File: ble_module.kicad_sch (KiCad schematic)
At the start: 2 parts, among them U1 STM32WB55RCVx, Y1 Crystal

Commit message: 3/8/2025
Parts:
- added C1, C2, C3, C4: 6 pF, Capacitor_SMD:C_0603_1608Metric, symbol Device:C
- added J1, J11: Conn_01x06_Pin, Connector_PinHeader_2.54mm:PinHeader_1x06_P2.54mm_Vertical, symbol Connector:Conn_01x06_Pin
- added J10: Conn_01x04_Pin, Connector_PinHeader_2.54mm:PinHeader_1x04_P2.54mm_Vertical, symbol Connector:Conn_01x04_Pin
- added J2: Conn_02x05_Odd_Even, Connector_PinHeader_1.27mm:PinHeader_2x05_P1.27mm_Vertical, symbol Connector_Generic:Conn_02x05_Odd_Even
- added J8: Conn_01x02_Pin, Connector_PinHeader_2.54mm:PinHeader_1x02_P2.54mm_Vertical, symbol Connector:Conn_01x02_Pin
- added J9: Conn_01x06_Pin, Connector_PinHeader_2.54mm:PinHeader_2x03_P2.54mm_Vertical, symbol Connector:Conn_01x06_Pin
- added R1, R2: 10k, Resistor_SMD:R_0603_1608Metric, symbol Device:R_US
- added SW1: PTS526 SK15 SMTR2 LFS, jka_library:PTS526SK15SMTR2 LFS, symbol jka_library:PTS526_SK15_SMTR2_LFS
- added Y1: ECS-320-8-33-RWY-TR, jka_library:XTAL_ECS-320-8-33-RWY-TR, symbol jka_library:ECS-320-8-33-RWY-TR
- Y2: renamed from Y1; value Crystal -> ECS-.327-9-12R-TR; footprint (none) -> Crystal:Crystal_SMD_2012-2Pin_2.0x1.2mm_HandSoldering
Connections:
- net +3.3V is gone; now on net +3V3: U1.14 (VDDA), U1.30 (VDD), U1.33 (VDDRF), U1.41 (VFBSMPS), U1.43 (VLXSMPS), U1.45 (VDD), U1.55 (VDDUSB), U1.68 (VDD)
- net I2C_SCL: now also U1.66 (PB6), J8.2 (Pin_2), R1.2
- net I2C_SDA: now also U1.67 (PB7), J8.1 (Pin_1), R2.2
- net OSC32_IN: now also Y2.2, C2.1
- net OSC32_OUT: now also Y2.1, C4.1
- net SAI_SD_A: now reaches U1.12 (PC3)
- net +3V3: now reaches U1.13 (VREF+)
- net +3V3: now also J11.3 (Pin_3), J2.1 (Pin_1), R1.1, R2.1
- net SPI1_SCK: now reaches U1.16 (PA1)
- net SPI1_SCK: now also J10.3 (Pin_3)
- net QSPI_NCS: now reaches U1.17 (PA2)
- net QSPI_NCS: now also J9.6 (Pin_6)
- net QSPI_CLK: now reaches U1.18 (PA3)
- net QSPI_CLK: now also J9.1 (Pin_1)
- net SPI1_NSS: now reaches U1.19 (PA4)
- net SPI1_NSS: now also J10.1 (Pin_1)
- net QSPI_IO3: now reaches U1.21 (PA6)
- net QSPI_IO3: now also J9.4 (Pin_4)
- net QSPI_IO2: now reaches U1.22 (PA7)
- net QSPI_IO2: now also U1.7 (PB9), J9.3 (Pin_3)
- net MCLK_OUT: now reaches U1.23 (PA8)
- net USART_TX: now reaches U1.24 (PA9)
- net USART_TX: now also J11.5 (Pin_5)
- net RF1: now reaches U1.31 (RF1)
- net GND: now reaches U1.32 (VSSRF)
- net GND: now also U1.69 (VSS), C1.2, C2.2, C3.2, C4.2, J1.3 (Pin_3), J11.1 (Pin_1), J2.3 (Pin_3), J2.5 (Pin_5), J2.9 (Pin_9), SW1.3, SW1.4, Y1.2 (GND), Y1.4 (GND__1)
- net OSC_OUT: now reaches U1.34 (OSC_OUT)
- net OSC_OUT: now also C3.1, Y1.3 (OUT/IN)
- net OSC_IN: now reaches U1.35 (OSC_IN)
- net OSC_IN: now also C1.1, Y1.1 (IN/OUT)
- net RX_TX_MOD_EXT_PA: now reaches U1.38 (PB0)
- net SAI_FS_A: now reaches U1.46 (PB12)
- net SAI_SCK_A: now reaches U1.47 (PB13)
- net SAI_MCLK_A: now reaches U1.48 (PB14)
- net BOOT0: now reaches U1.5 (PH3)
- net USART_RX: now reaches U1.51 (PA10)
- net USART_RX: now also J11.4 (Pin_4)
- net USB_D-: now reaches U1.52 (PA11)
- net USB_D+: now reaches U1.53 (PA12)
- net JTMS_SWDIO: now reaches U1.54 (PA13)
- net JTMS_SWDIO: now also J1.4 (Pin_4), J2.2 (Pin_2)
- net JTCLK_SWCLK: now reaches U1.56 (PA14)
- net JTCLK_SWCLK: now also J1.5 (Pin_5), J2.4 (Pin_4)
- net QSPI_IO1: now reaches U1.6 (PB8)
- net QSPI_IO1: now also J9.2 (Pin_2)
- net SPI1_MISO: now reaches U1.64 (PB4)
- net SPI1_MISO: now also J10.4 (Pin_4)
- net SPI1_MOSI: now reaches U1.65 (PB5)
- net SPI1_MOSI: now also J10.2 (Pin_2)
- net STM_NRST: now reaches U1.8 (NRST)
- net STM_NRST: now also SW1.1, SW1.2
- new net NRST: J2.10 (Pin_10)
- new net QSPI_IO4: J9.5 (Pin_5)
- new net RESET: J1.1 (Pin_1)
- new net SWO: J2.6 (Pin_6)
- new net USART_CTS: J11.2 (Pin_2)
- new net USART_RTS: J11.6 (Pin_6)
- new net VDD: J1.2 (Pin_2)
- no-connect marks 0 -> 6
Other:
- added sheet Analog Sensing (Analog_Sensing.kicad_sch)
- added sheet Audio (Audio.kicad_sch)
- added sheet RF Block (RF_Block.kicad_sch)
- added sheet STM Decoupling Capacitors (STM_Decoupling_Caps.kicad_sch)
- sheet Character Display ports: added DB0, DB1, DB2, DB3, DB4, DB5, DB6, DB7, LCD_EN, REG_SEL, R/W; removed none
- sheet DC-DC Converter ports: added +1V8, +1V8_EN, +5V, +5V_EN, GND; removed none
- sheet Power ports: added USB_D+, USB_D-; removed none
- sheet Serial Memory ports: added EEPROM_WP, I2C_SCL, I2C_SDA, QSPI_CLK, QSPI_FLASH_CS, QSPI_SIO0, QSPI_SIO1, QSPI_SIO2, QSPI_SIO3, SPI_CLK, SPI_DI, SPI_DO, SPI_SD_CS; removed none
- note added: "32 MHz"
- note added: "Not needed due to internal caps?"

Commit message: Layout draft complete
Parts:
- removed C1, C2, C3, C4: 6 pF, Capacitor_SMD:C_0603_1608Metric, symbol Device:C
- removed J1, J11: Conn_01x06_Pin, Connector_PinHeader_2.54mm:PinHeader_1x06_P2.54mm_Vertical, symbol Connector:Conn_01x06_Pin
- removed J10: Conn_01x04_Pin, Connector_PinHeader_2.54mm:PinHeader_1x04_P2.54mm_Vertical, symbol Connector:Conn_01x04_Pin
- removed J2: Conn_02x05_Odd_Even, Connector_PinHeader_1.27mm:PinHeader_2x05_P1.27mm_Vertical, symbol Connector_Generic:Conn_02x05_Odd_Even
- removed J8: Conn_01x02_Pin, Connector_PinHeader_2.54mm:PinHeader_1x02_P2.54mm_Vertical, symbol Connector:Conn_01x02_Pin
- removed J9: Conn_01x06_Pin, Connector_PinHeader_2.54mm:PinHeader_2x03_P2.54mm_Vertical, symbol Connector:Conn_01x06_Pin
- removed R1, R2: 10k, Resistor_SMD:R_0603_1608Metric, symbol Device:R_US
- removed SW1: PTS526 SK15 SMTR2 LFS, jka_library:PTS526SK15SMTR2 LFS, symbol jka_library:PTS526_SK15_SMTR2_LFS
- removed U1: STM32WB55RCVx, Package_DFN_QFN:QFN-68-1EP_8x8mm_P0.4mm_EP6.4x6.4mm, symbol MCU_ST_STM32WB:STM32WB55RCVx
- removed Y1: ECS-320-8-33-RWY-TR, jka_library:XTAL_ECS-320-8-33-RWY-TR, symbol jka_library:ECS-320-8-33-RWY-TR
- removed Y2: ECS-.327-9-12R-TR, Crystal:Crystal_SMD_2012-2Pin_2.0x1.2mm_HandSoldering, symbol Device:Crystal
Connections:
- no-connect marks 6 -> 0
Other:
- added sheet Controller (Controller.kicad_sch)
- added sheet Headers (Headers.kicad_sch)
- sheet Analog Sensing ports: added none; removed I2C_SCL, I2C_SDA, TEMP_ALERT
- sheet Audio ports: added none; removed GPIO/DOUT, I2C_SCL, I2C_SDA, I2S_BCLK, I2S_DIN, I2S_WCLK, MCLK, ~{RST}
- sheet Character Display ports: added none; removed DB0, DB1, DB2, DB3, DB4, DB5, DB6, DB7, LCD_EN, REG_SEL, R/W
- sheet DC-DC Converter ports: added none; removed +1V8, +1V8_EN, +5V, +5V_EN, 3.3V, GND, VIN
- sheet Power ports: added none; removed 3V3-RTC, I2C_SCL, I2C_SDA, USB_D+, USB_D-, VBUS_MAIN, VBUS_SENSE
- sheet RF Block ports: added none; removed RF1
- sheet Serial Memory ports: added none; removed EEPROM_WP, I2C_SCL, I2C_SDA, QSPI_CLK, QSPI_FLASH_CS, QSPI_SIO0, QSPI_SIO1, QSPI_SIO2, QSPI_SIO3, SPI_CLK, SPI_DI, SPI_DO, SPI_SD_CS
- note added: "Audio and Visual"
- note added: "Header Connections"
- note added: "Memory"
- note added: "Power and Regulation"
- note added: "STM32 Controller"
- note removed: "32 MHz"
- note removed: "DONE"
- note removed: "Not needed due to internal caps?"
- note removed: "When using LDO mode for input power VDDSMPS, VLXSMPS, and VFBSMPS should be connected to VDD"
- title: (none) -> Jakka1

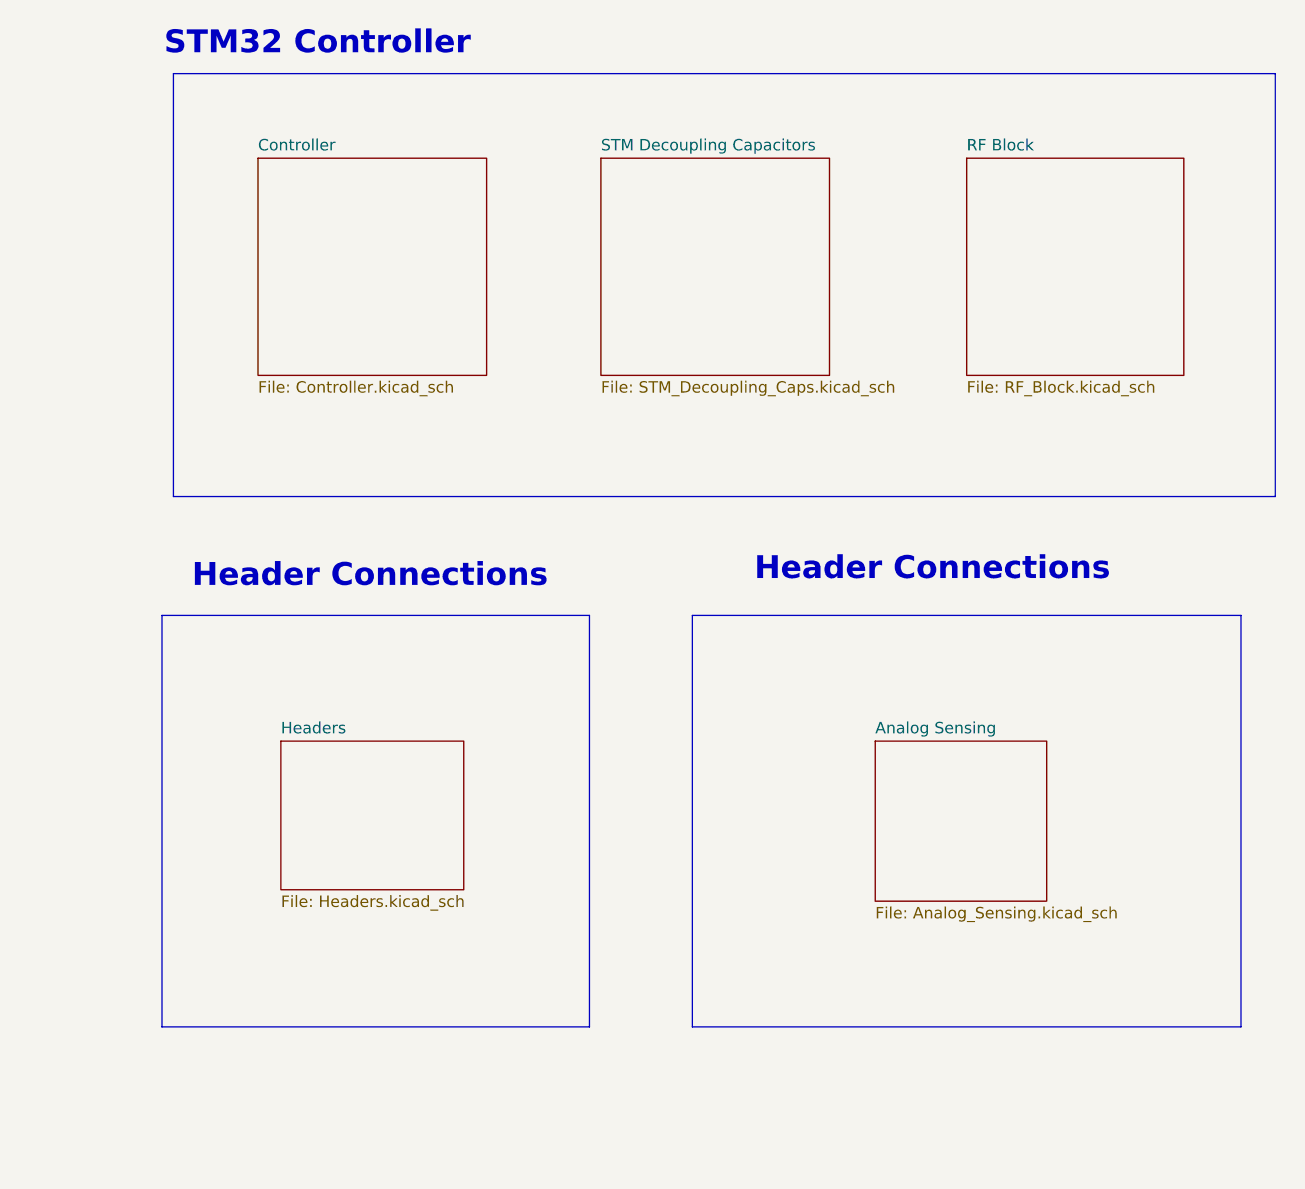
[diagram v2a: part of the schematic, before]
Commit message: First draft of design output, schematic, and layout complete
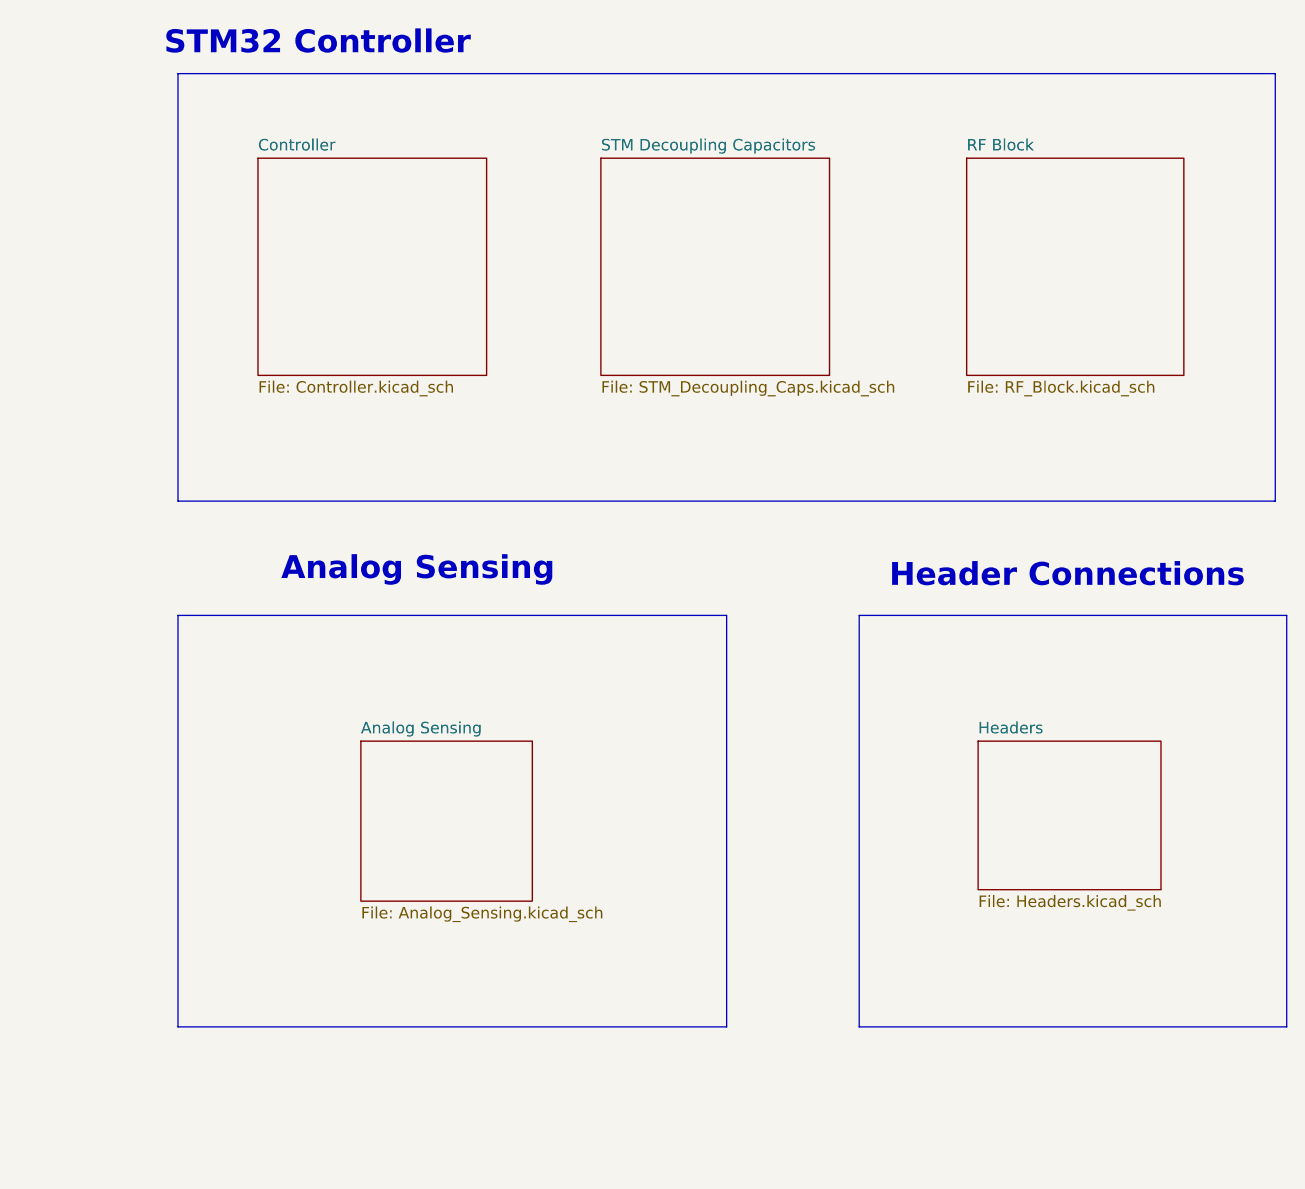
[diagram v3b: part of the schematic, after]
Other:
- note added: "Analog Sensing"
- company: (none) -> Jacob Kapala
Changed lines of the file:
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@@
 		(date "2025-03-31")
 		(rev "1")
-	)
-	(rectangle
-		(start 207.01 85.09)
-		(end 267.97 130.81)
-		(stroke
-			(width 0)
-			(type default)
-		)
-		(fill
-			(type none)
-		)
-	)
-	(rectangle
-		(start 149.352 24.892)
-		(end 271.78 71.882)
+		(company "Jacob Kapala")
+	)
+	(rectangle
+		(start 149.86 85.09)
+		(end 210.82 130.81)
+		(stroke
+			(width 0)
+			(type default)
+		)
+		(fill
+			(type none)
+		)
+	)
+	(rectangle
+		(start 149.86 24.892)
+		(end 271.78 72.39)
 		(stroke
 			(width 0)
@@
 	)
 	(rectangle
-		(start 148.082 85.09)
-		(end 195.58 130.81)
+		(start 225.552 85.09)
+		(end 273.05 130.81)
 		(stroke
 			(width 0)
@@
 	(text "Header Connections"
 		(exclude_from_sim no)
-		(at 171.196 80.772 0)
+		(at 248.666 80.772 0)
 		(effects
 			(font
@@
 		)
 	)
-	(text "Header Connections"
-		(exclude_from_sim no)
-		(at 233.68 80.01 0)
+	(text "Analog Sensing"
+		(exclude_from_sim no)
+		(at 176.53 80.01 0)
 		(effects
 			(font
@@
 	)
 	(sheet
-		(at 161.29 99.06)
+		(at 238.76 99.06)
 		(size 20.32 16.51)
 		(fields_autoplaced yes)
@@
 		)
 		(property "Sheetname" "Headers"
-			(at 161.29 98.3484 0)
+			(at 238.76 98.3484 0)
 			(effects
 				(font
@@
 		)
 		(property "Sheetfile" "Headers.kicad_sch"
-			(at 161.29 116.1546 0)
+			(at 238.76 116.1546 0)
 			(effects
 				(font
@@
 	)
 	(sheet
-		(at 227.33 99.06)
+		(at 170.18 99.06)
 		(size 19.05 17.78)
 		(fields_autoplaced yes)
@@
 		)
 		(property "Sheetname" "Analog Sensing"
-			(at 227.33 98.3484 0)
+			(at 170.18 98.3484 0)
 			(effects
 				(font
@@
 		)
 		(property "Sheetfile" "Analog_Sensing.kicad_sch"
-			(at 227.33 117.4246 0)
-			(effects
-				(font
+			(at 170.18 117.4246 0)
+			(effects
+				(font
